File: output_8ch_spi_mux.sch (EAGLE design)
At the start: 35 parts, among them IC1 TPS706-1V8, IC2 SN75174PDIP-16, IC3 5M160ZE64, IC5 SN75174PDIP-16, Q1 50MHz

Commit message: added mostly complete board for mux
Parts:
- removed C18, C19: 100nF, rcl:C-EUC0805
- removed C21: 47µF, rcl:CPOL-EUCT6032
- removed SV3, SV4: 1792928, lichtenstein_onion:1792928
- added K1: PIN20X2, FLYFISH:PIN20X2
- added LED3, LED4: (no value), led:LEDCHIPLED_1206
- added R3: 680R, rcl:R-EU_M0805
- added R4: 0R, rcl:R-EU_M0805
- added R5: 1k, rcl:R-EU_M0805
- added R6, R7: 3k9, rcl:R-EU_M0805
- added SJ1: (no value), jumper:SJ
- added U1: CAT24C256, FLYFISH:EEPROM24
- C11: value 47µF -> 4.7µF; device rcl:CPOL-EUCT6032 -> rcl:C-EUC0805; MOUSER 581-TAJD476M016RNJV -> 81-GRM21BR71A475ME1L
- C12: value 4.7µF -> 100nF; MOUSER 81-GRM21BR71A475ME1L -> 710-885012207072
- IC2: value SN75174PDIP-16 -> 5M160ZE64; device lichtenstein_onion:SN75174PDIP-16 -> lichtenstein_onion:5M160ZE64
- IC3: value 5M160ZE64 -> SN75174SOIC-20; device lichtenstein_onion:5M160ZE64 -> lichtenstein_onion:SN75174SOIC-20
- IC4: value (none) -> SN75174SOIC-20; device lichtenstein_onion:TXB0108TSSOP20 -> lichtenstein_onion:SN75174SOIC-20
- IC5: value SN75174PDIP-16 -> (none); device lichtenstein_onion:SN75174PDIP-16 -> lichtenstein_onion:TXB0108TSSOP20
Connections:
- removed net V+: C16.1, C17.1, C18.1, IC4.VCCB
- new net ID_SCL: K1.28, R7.1, U1.SCL
- new net ID_SDA: K1.27, R6.1, U1.SDA
- new net N$1: LED4.A, R4.2
- new net N$2: LED3.A, R3.2
- new net N$3: R5.1, SJ1.1, U1.WP
- new net OUT01_OE: IC2.IO32
- new net OUT23_OE: IC2.IO31
- new net OUT45_OE: IC2.IO30
- new net OUT67_OE: IC2.IO29
- new net STATUS2: IC2.IO54, R3.1
- net !OUT_ENABLE: now also IC2.IO12, K1.13; no longer IC3.IO2, SV2.14
- net !OUT_RESET: now also IC2.IO13, K1.11; no longer IC3.IO1, SV2.16
- net !SPI_CS: now also IC2.IO4, K1.24; no longer IC3.IO3, SV2.6
- net +3V3: now also C17.1, IC2.VCCIO1, IC2.VCCIO2, IC5.VCCA, K1.1, K1.17, R5.2, R6.2, R7.2, U1.VCC; no longer C11.+, C14.1, C3.1, C6.+, IC3.VCCIO1, IC3.VCCIO2, IC4.VCCA, SV2.2, SV2.4
- net +5V: now also C13.1, C14.1, C16.1, C3.1, C6.+, IC3.VCC, IC4.VCC, IC5.VCCB, K1.2, K1.4, SV2.2, SV2.4; no longer C19.1, C21.+, IC2.VCC, IC5.VCC
- net BUFFER_OE: now also IC2.IO33, IC5.OE; no longer IC3.IO46, IC4.OE
- net CLK_50: now also IC2.CLK0; no longer IC3.CLK0
- net CPLD_TCK: now also IC2.TCK; no longer IC3.TCK
- net CPLD_TDI: now also IC2.TDI; no longer IC3.TDI
- net CPLD_TDO: now also IC2.TDO; no longer IC3.TDO
- net CPLD_TMS: now also IC2.TMS; no longer IC3.TMS
- net GND: now also C11.2, K1.14, K1.20, K1.25, K1.30, K1.34, K1.39, K1.6, K1.9, LED3.C, LED4.C, SJ1.2, U1.A0, U1.A1, U1.A2, U1.GND; no longer C11.-, C18.2, C19.2, C21.-, SV2.11, SV2.13, SV2.15, SV2.17, SV2.19, SV2.5, SV2.7, SV2.9
- net I2C_SCL: now also K1.5; no longer SV2.20
- net I2C_SDA: now also K1.3; no longer SV2.18
- net OUT01_EN: now also IC4.EN12; no longer IC2.EN12, IC3.IO47
- net OUT0_N: now also IC4.Z1, SV2.8; no longer IC2.Z1, SV3.2
- net OUT0_P: now also IC4.Y1, SV2.6; no longer IC2.Y1, SV3.1
- net OUT1_N: now also IC4.Z2, SV2.12; no longer IC2.Z2, SV3.4
- net OUT1_P: now also IC4.Y2, SV2.10; no longer IC2.Y2, SV3.3
- net OUT23_EN: now also IC4.EN34; no longer IC2.EN34, IC3.IO48
- net OUT2_N: now also IC4.Z3, SV2.16; no longer IC2.Z3, SV3.6
- net OUT2_P: now also IC4.Y3, SV2.14; no longer IC2.Y3, SV3.5
- net OUT3_N: now also IC4.Z4, SV2.20; no longer IC2.Z4, SV3.8
- net OUT3_P: now also IC4.Y4, SV2.18; no longer IC2.Y4, SV3.7
- net OUT45_EN: now also IC3.EN12; no longer IC3.IO49, IC5.EN12
- net OUT4_N: now also IC3.Z1, SV2.7; no longer IC5.Z1, SV4.2
- net OUT4_P: now also IC3.Y1, SV2.5; no longer IC5.Y1, SV4.1
- net OUT5_N: now also IC3.Z2, SV2.11; no longer IC5.Z2, SV4.4
- net OUT5_P: now also IC3.Y2, SV2.9; no longer IC5.Y2, SV4.3
- net OUT67_EN: now also IC3.EN34; no longer IC3.IO50, IC5.EN34
- net OUT6_N: now also IC3.Z3, SV2.15; no longer IC5.Z3, SV4.6
- net OUT6_P: now also IC3.Y3, SV2.13; no longer IC5.Y3, SV4.5
- net OUT7_N: now also IC3.Z4, SV2.19; no longer IC5.Z4, SV4.8
- net OUT7_P: now also IC3.Y4, SV2.17; no longer IC5.Y4, SV4.7
- net OUTPUT0: now also IC4.A1, IC5.B1; no longer IC2.A1, IC4.B1
- net OUTPUT1: now also IC4.A2, IC5.B2; no longer IC2.A2, IC4.B2
- net OUTPUT2: now also IC4.A3, IC5.B3; no longer IC2.A3, IC4.B3
- net OUTPUT3: now also IC4.A4, IC5.B4; no longer IC2.A4, IC4.B4
- net OUTPUT4: now also IC3.A1, IC5.B5; no longer IC4.B5, IC5.A1
- net OUTPUT5: now also IC3.A2, IC5.B6; no longer IC4.B6, IC5.A2
- net OUTPUT6: now also IC3.A3, IC5.B7; no longer IC4.B7, IC5.A3
- net OUTPUT7: now also IC3.A4, IC5.B8; no longer IC4.B8, IC5.A4
- net OUT_3V0: now also IC2.IO45, IC5.A1; no longer IC3.IO34, IC4.A1
- net OUT_3V1: now also IC2.IO44, IC5.A2; no longer IC3.IO35, IC4.A2
- net OUT_3V2: now also IC2.IO43, IC5.A3; no longer IC3.IO36, IC4.A3
- net OUT_3V3: now also IC2.IO38, IC5.A4; no longer IC3.IO37, IC4.A4
- net OUT_3V4: now also IC2.IO37, IC5.A5; no longer IC3.IO38, IC4.A5
- net OUT_3V5: now also IC2.IO36, IC5.A6; no longer IC3.IO43, IC4.A6
- net OUT_3V6: now also IC2.IO35, IC5.A7; no longer IC3.IO44, IC4.A7
- net OUT_3V7: now also IC2.IO34, IC5.A8; no longer IC3.IO45, IC4.A8
- net SPI_MISO: now also IC2.IO10, K1.21; no longer IC3.IO4, SV2.12
- net SPI_MOSI: now also IC2.IO11, K1.19; no longer IC3.IO5, SV2.10
- net SPI_SCK: now also IC2.IO5, K1.23; no longer IC3.IO10, SV2.8
- net STATUS0: now also IC2.IO55; no longer IC3.IO11
- net STATUS1: now also IC2.IO56; no longer IC3.IO12
- net VCORE: now also C11.1, IC2.VCCINT, R4.1; no longer C13.1, IC3.VCCINT
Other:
- note removed: "Main Board Connector"

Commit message: routed missing differential driver enables
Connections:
- removed net OUT01_OE: IC2.IO32
- removed net OUT23_OE: IC2.IO31
- removed net OUT45_OE: IC2.IO30
- removed net OUT67_OE: IC2.IO29
- net OUT01_EN: now also IC2.IO32
- net OUT23_EN: now also IC2.IO31
- net OUT45_EN: now also IC2.IO30
- net OUT67_EN: now also IC2.IO29
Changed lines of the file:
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@@
 <junction x="170.18" y="104.14"/>
+</segment>
+<segment>
+<pinref part="IC2" gate="G$1" pin="IO29"/>
+<wire x1="73.66" y1="99.06" x2="68.58" y2="99.06" width="0.1524" layer="91"/>
+<label x="68.58" y="99.06" size="1.27" layer="95" rot="R180" xref="yes"/>
 </segment>
 </net>
@@
 <junction x="170.18" y="101.6"/>
 </segment>
+<segment>
+<pinref part="IC2" gate="G$1" pin="IO30"/>
+<wire x1="68.58" y1="96.52" x2="73.66" y2="96.52" width="0.1524" layer="91"/>
+<label x="68.58" y="96.52" size="1.27" layer="95" rot="R180" xref="yes"/>
+</segment>
 </net>
 <net name="OUT23_EN" class="0">
@@
 <junction x="170.18" y="66.04"/>
 </segment>
+<segment>
+<pinref part="IC2" gate="G$1" pin="IO31"/>
+<wire x1="73.66" y1="93.98" x2="68.58" y2="93.98" width="0.1524" layer="91"/>
+<label x="68.58" y="93.98" size="1.27" layer="95" rot="R180" xref="yes"/>
+</segment>
 </net>
 <net name="OUT01_EN" class="0">
@@
 <label x="175.26" y="63.5" size="1.27" layer="95" xref="yes"/>
 <junction x="170.18" y="63.5"/>
+</segment>
+<segment>
+<pinref part="IC2" gate="G$1" pin="IO32"/>
+<wire x1="73.66" y1="91.44" x2="68.58" y2="91.44" width="0.1524" layer="91"/>
+<label x="68.58" y="91.44" size="1.27" layer="95" rot="R180" xref="yes"/>
 </segment>
 </net>
@@
 </segment>
 </net>
-<net name="OUT01_OE" class="0">
-<segment>
-<pinref part="IC2" gate="G$1" pin="IO32"/>
-<wire x1="73.66" y1="91.44" x2="68.58" y2="91.44" width="0.1524" layer="91"/>
-<label x="68.58" y="91.44" size="1.27" layer="95" rot="R180" xref="yes"/>
-</segment>
-</net>
-<net name="OUT23_OE" class="0">
-<segment>
-<pinref part="IC2" gate="G$1" pin="IO31"/>
-<wire x1="73.66" y1="93.98" x2="68.58" y2="93.98" width="0.1524" layer="91"/>
-<label x="68.58" y="93.98" size="1.27" layer="95" rot="R180" xref="yes"/>
-</segment>
-</net>
-<net name="OUT45_OE" class="0">
-<segment>
-<pinref part="IC2" gate="G$1" pin="IO30"/>
-<wire x1="68.58" y1="96.52" x2="73.66" y2="96.52" width="0.1524" layer="91"/>
-<label x="68.58" y="96.52" size="1.27" layer="95" rot="R180" xref="yes"/>
-</segment>
-</net>
-<net name="OUT67_OE" class="0">
-<segment>
-<pinref part="IC2" gate="G$1" pin="IO29"/>
-<wire x1="73.66" y1="99.06" x2="68.58" y2="99.06" width="0.1524" layer="91"/>
-<label x="68.58" y="99.06" size="1.27" layer="95" rot="R180" xref="yes"/>
-</segment>
-</net>

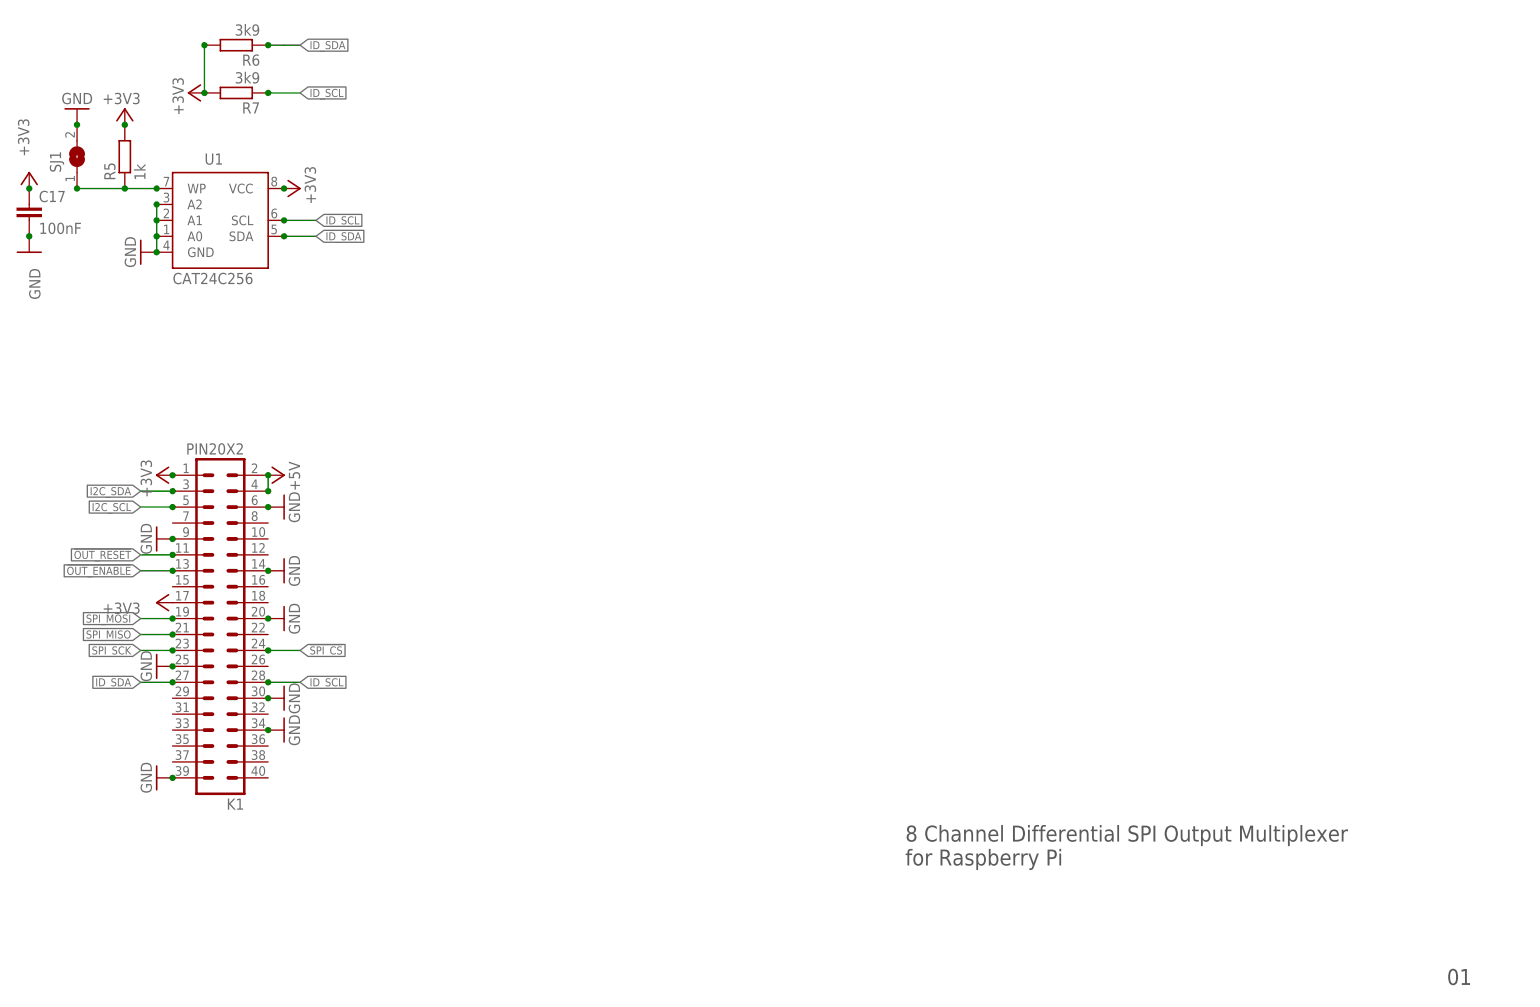
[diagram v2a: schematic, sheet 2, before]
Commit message: Added MCP2517FD CAN transceiver
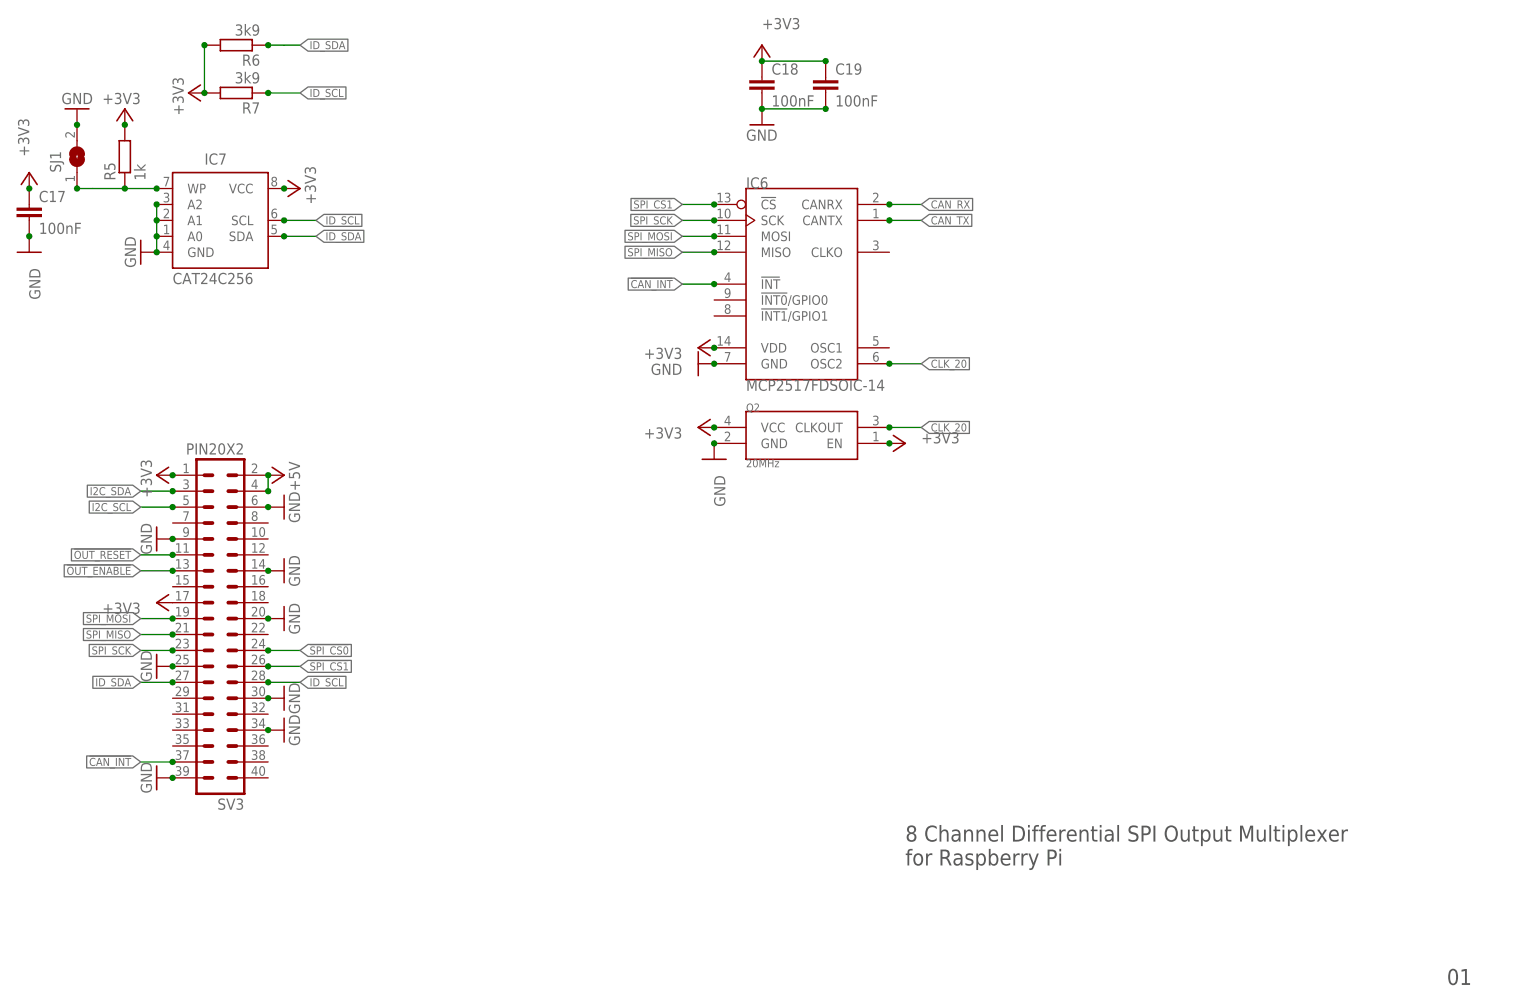
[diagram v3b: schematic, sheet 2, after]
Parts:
- added C18, C19: 100nF, rcl:C-EUC0805
- added IC6: MCP2517FDSOIC-14, lichtenstein_onion:MCP2517FDSOIC-14
- added Q2: 20MHz, lichtenstein_onion:DSC61XX
- SV2: device con-lstb:MA10-2 -> con-lstb:MA12-2
- renumbered K1 to SV3, U1 to IC7
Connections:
- net !SPI_CS renamed !SPI_CS0
- new net !CAN_INT: IC6.!INT, SV3.37
- new net !SPI_CS1: IC6.!CS, SV3.26
- new net CAN_RX: IC6.CANRX, SV2.23
- new net CAN_TX: IC6.CANTX, SV2.24
- new net CLK_20: IC6.OSC2, Q2.CLKOUT
- net +3V3: now also C18.1, C19.1, IC6.VDD, Q2.EN, Q2.VCC, SV2.2
- net +5V: no longer SV2.2
- net GND: now also C18.2, C19.2, IC6.GND, Q2.GND, SV2.21, SV2.22
- net SPI_MISO: now also IC6.MISO
- net SPI_MOSI: now also IC6.MOSI
- net SPI_SCK: now also IC6.SCK

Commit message: Added STM32 as CAN bus controller to rpi board
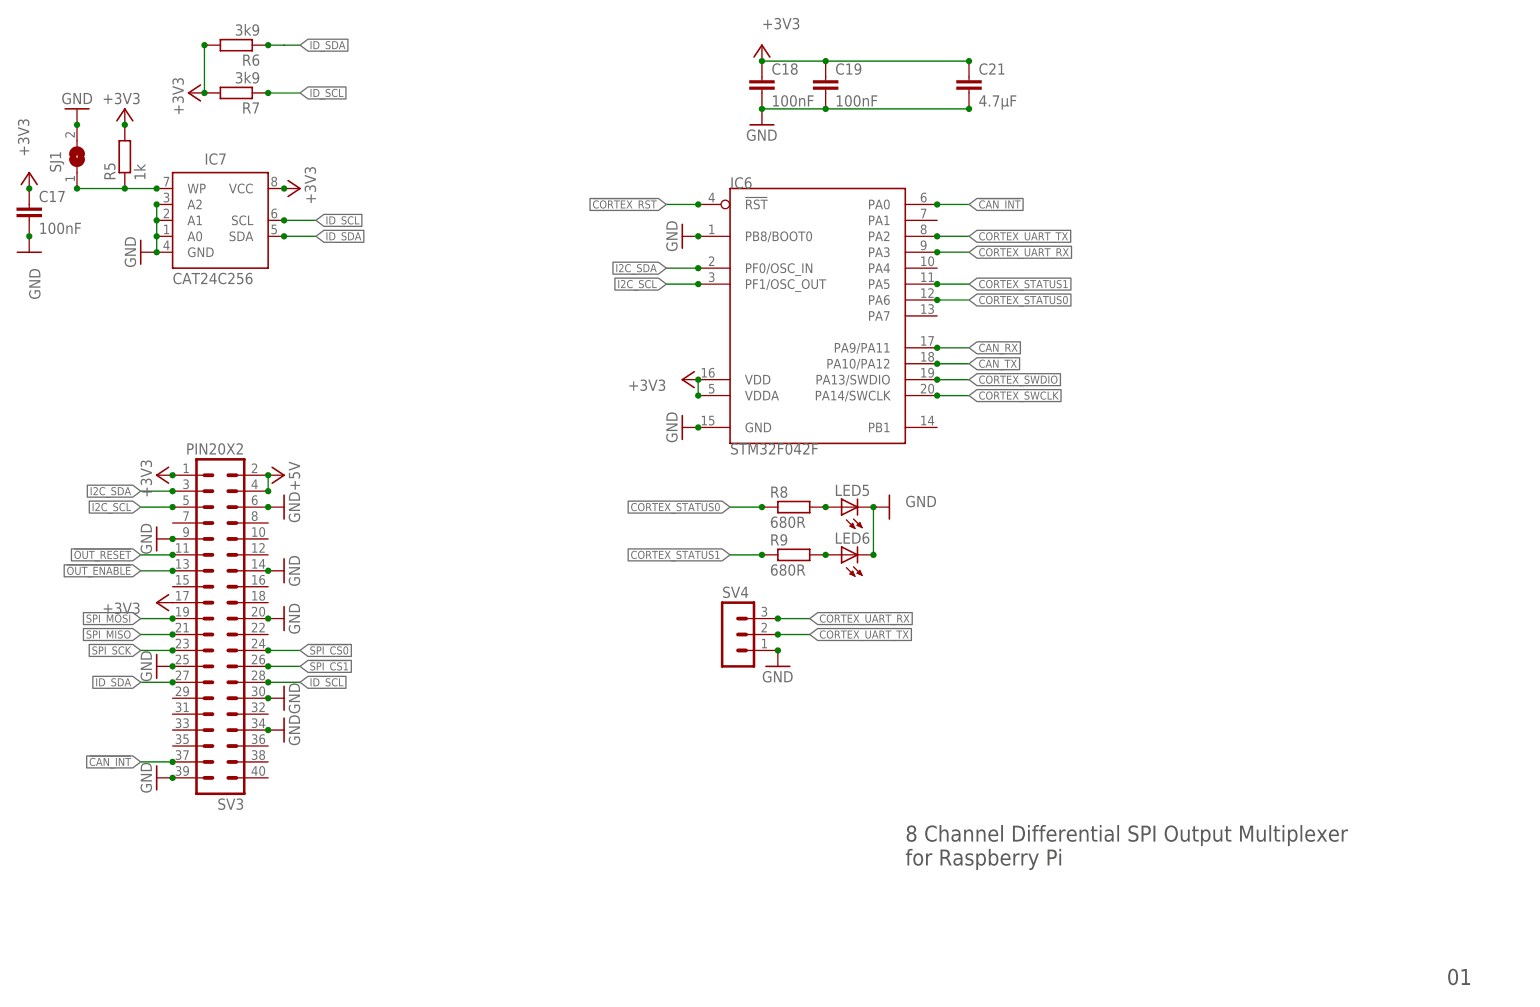
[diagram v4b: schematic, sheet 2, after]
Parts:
- removed Q2: 20MHz, lichtenstein_onion:DSC61XX
- added C21: 4.7µF, rcl:C-EUC0805
- added LED5, LED6: (no value), led:LEDCHIPLED_1206
- added R8, R9: 680R, rcl:R-EU_M0805
- added SV4: (no value), con-lstb:MA03-1
- IC6: value MCP2517FDSOIC-14 -> STM32F042F; device lichtenstein_onion:MCP2517FDSOIC-14 -> lichtenstein_onion:STM32F042F
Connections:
- removed net CLK_20: IC6.OSC2, Q2.CLKOUT
- new net !CORTEX_RST: IC6.!RST
- new net CORTEX_STATUS0: IC6.PA6, R8.1
- new net CORTEX_STATUS1: IC6.PA5, R9.1
- new net CORTEX_SWCLK: IC6.PA14/SWCLK
- new net CORTEX_SWDIO: IC6.PA13/SWDIO
- new net CORTEX_UART_RX: IC6.PA3, SV4.3
- new net CORTEX_UART_TX: IC6.PA2, SV4.2
- new net N$4: LED5.A, R8.2
- new net N$5: LED6.A, R9.2
- net !CAN_INT: now also IC6.PA0; no longer IC6.!INT
- net !SPI_CS1: no longer IC6.!CS
- net +3V3: now also C21.1, IC6.VDDA; no longer Q2.EN, Q2.VCC
- net CAN_RX: now also IC6.PA9/PA11; no longer IC6.CANRX
- net CAN_TX: now also IC6.PA10/PA12; no longer IC6.CANTX
- net GND: now also C21.2, IC6.PB8/BOOT0, LED5.C, LED6.C, SV4.1; no longer Q2.GND
- net I2C_SCL: now also IC6.PF1/OSC_OUT
- net I2C_SDA: now also IC6.PF0/OSC_IN
- net SPI_MISO: no longer IC6.MISO
- net SPI_MOSI: no longer IC6.MOSI
- net SPI_SCK: no longer IC6.SCK
